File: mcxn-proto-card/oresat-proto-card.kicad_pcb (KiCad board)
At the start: 4 copper layers, 99.8 x 94.6 mm, 123 parts, among them J1 J-SAMTEC-TFM-110-01-L-D-RA, J2 U.FL, J3 U.FL, J4 U.FL, J6 J-SAMTEC-TFM-120-X1-XXX-D-RA, J7 ORESAT-DEBUG-CONNECTOR-ALL, Q1 DMP2240UDM, Q2 DMP3050LVT-7, Q7 MOSFET-PCH-SOT23-6, Q8 PMV45EN, Q9 PMV45EN, U10 TPS62111RSA, U11 MIC842LYC5, U12 MIC842LYC5, U2 MAX7310, U3 TS5A21366DCUR, U4 TCAN330, U6 MAX4211, U7 STM32F091C, X2 CRYSTAL-WITH-GND

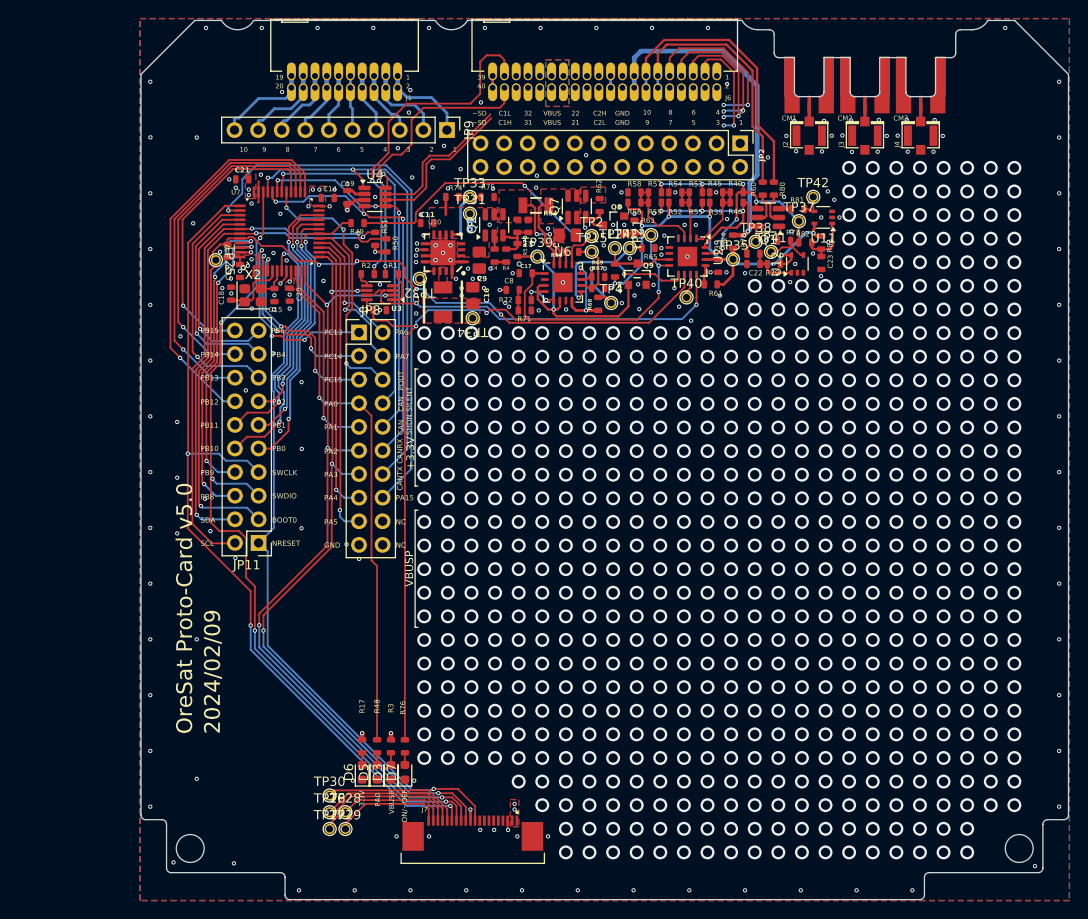
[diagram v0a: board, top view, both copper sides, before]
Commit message: Updated TPS62111RSA
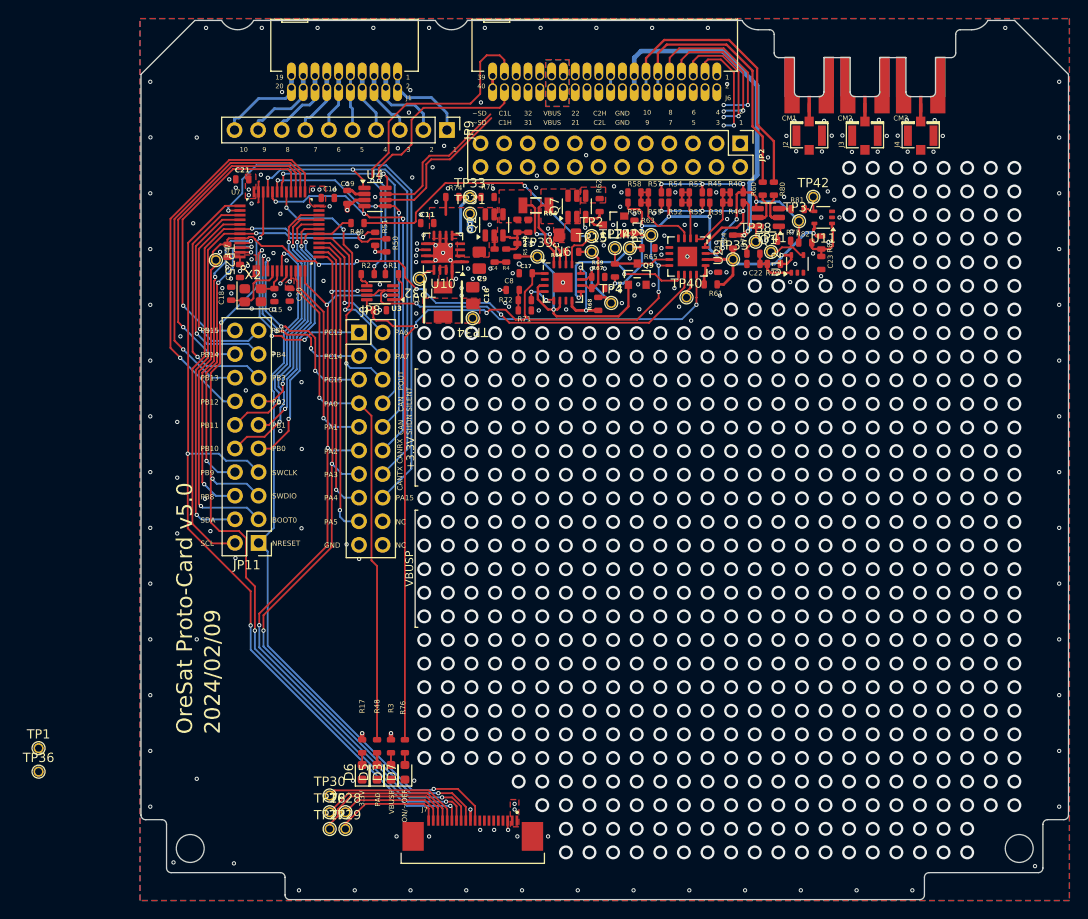
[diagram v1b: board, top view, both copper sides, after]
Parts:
- added TP1: Test-Point, oresat-misc:TestPoint-0.75mm-th, F.Cu at (87.6, 136.0)
- added TP36: Test-Point, oresat-misc:TestPoint-0.75mm-th, F.Cu at (87.6, 138.5)
- Q8: footprint oresat-proto-card:SOT23 -> oresat-ics:SOT23
- U10: footprint oresat-proto-card:S-PVQFN-16 -> Package_DFN_QFN:QFN-16-1EP_4x4mm_P0.65mm_EP2.15x2.15mm

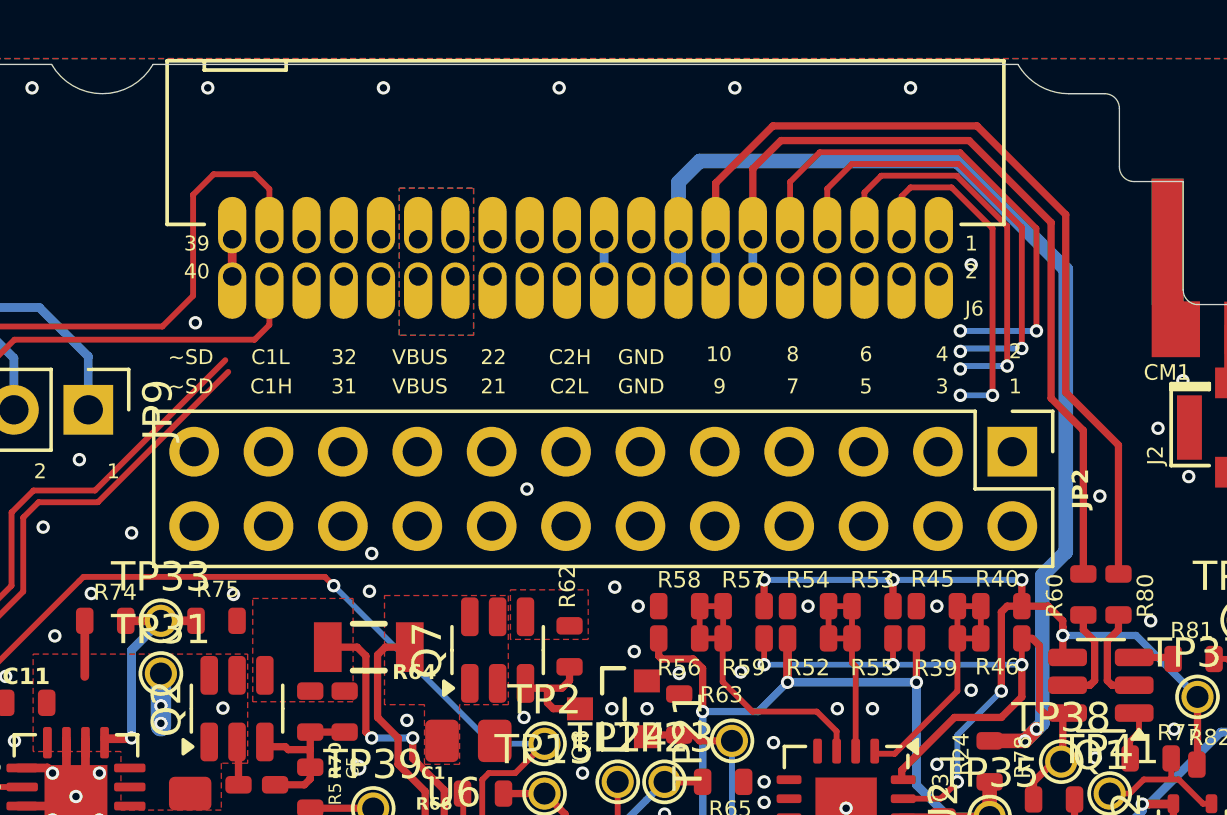
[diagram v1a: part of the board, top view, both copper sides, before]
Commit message: changed layout
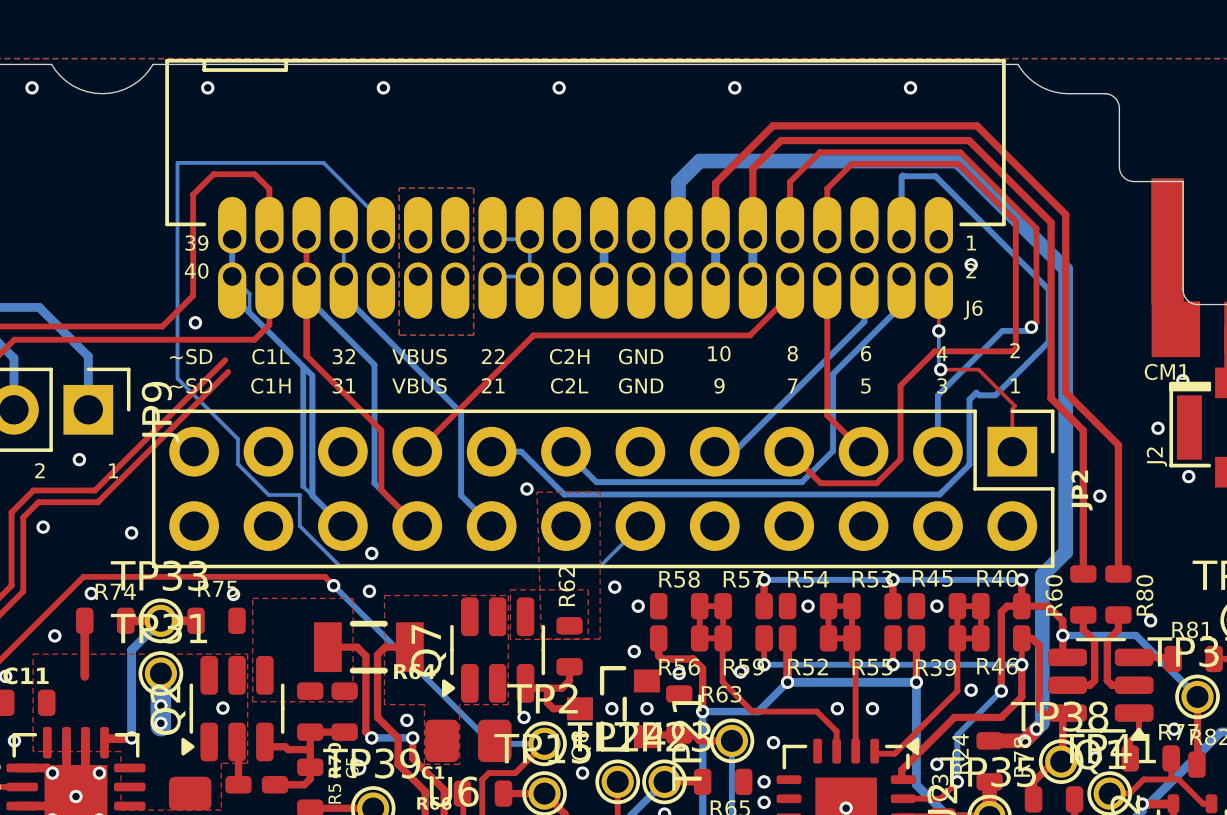
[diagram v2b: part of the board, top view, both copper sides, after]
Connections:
- JP2 pad 1: /Connectors/SPARE10 -> /Connectors/SPARE2
- JP2 pad 10: VBUS -> /Connectors/SPARE32
- JP2 pad 14: /Connectors/SPARE32 -> VBUS
- JP2 pad 17: /Connectors/SPARE2 -> /Connectors/SPARE10
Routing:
- net /Connectors/SPARE31: track 0.00 -> 35.9 mm
- net /Connectors/CAN1_L: track 0.00 -> 25.4 mm
- net /Connectors/SPARE3: track 12.1 -> 33.7 mm, vias 2 -> 0
- net /Connectors/~{SD}: track 1.27 -> 22.7 mm
- net /Connectors/SPARE4: track 0.00 -> 16.9 mm
- net /Connectors/SPARE10: track 0.00 -> 15.6 mm
- net /Connectors/SPARE5: track 13.8 -> 0.00 mm, vias 2 -> 0
- net /Connectors/CAN1_H: track 0.00 -> 11.9 mm
- net /Connectors/SPARE7: track 15.9 -> 25.2 mm, vias 2 -> 0
- net /Connectors/SPARE6: track 0.00 -> 8.49 mm
- net /Connectors/SPARE2: track 0.00 -> 7.89 mm, vias 0 -> 2
- net /Connectors/SPARE8: track 0.00 -> 6.50 mm
- net VBUS: track 0.00 -> 3.81 mm
- net /Connectors/SPARE9: track 18.0 -> 21.4 mm, vias 2 -> 1
